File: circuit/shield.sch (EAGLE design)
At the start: 24 parts, among them Q1 BC547, Q2 BC547, Q3 BC547

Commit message: Removed useless pulldown resistors
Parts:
- removed R19: 10k, rcl:R-EU_0204/2V
- removed R20, R21: 10k, rcl:R-EU_0204/7
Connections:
- net GND: no longer R19.2, R20.2, R21.2
- net N$30: no longer R19.1
- net N$31: no longer R20.1
- net N$32: no longer R21.1
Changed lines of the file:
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@@
 <grid distance="0.1" unitdist="inch" unit="inch" style="lines" multiple="1" display="no" altdistance="0.01" altunitdist="inch" altunit="inch"/>
 <layers>
-<layer number="1" name="Top" color="4" fill="1" visible="yes" active="no"/>
-<layer number="16" name="Bottom" color="1" fill="1" visible="yes" active="no"/>
-<layer number="17" name="Pads" color="2" fill="1" visible="yes" active="no"/>
-<layer number="18" name="Vias" color="2" fill="1" visible="yes" active="no"/>
-<layer number="19" name="Unrouted" color="6" fill="1" visible="yes" active="no"/>
-<layer number="20" name="Dimension" color="15" fill="1" visible="yes" active="no"/>
-<layer number="21" name="tPlace" color="7" fill="1" visible="yes" active="no"/>
-<layer number="22" name="bPlace" color="7" fill="1" visible="yes" active="no"/>
-<layer number="23" name="tOrigins" color="15" fill="1" visible="yes" active="no"/>
-<layer number="24" name="bOrigins" color="15" fill="1" visible="yes" active="no"/>
-<layer number="25" name="tNames" color="7" fill="1" visible="yes" active="no"/>
-<layer number="26" name="bNames" color="7" fill="1" visible="yes" active="no"/>
-<layer number="27" name="tValues" color="7" fill="1" visible="yes" active="no"/>
-<layer number="28" name="bValues" color="7" fill="1" visible="yes" active="no"/>
+<layer number="1" name="Top" color="4" fill="1" visible="no" active="no"/>
+<layer number="16" name="Bottom" color="1" fill="1" visible="no" active="no"/>
+<layer number="17" name="Pads" color="2" fill="1" visible="no" active="no"/>
+<layer number="18" name="Vias" color="2" fill="1" visible="no" active="no"/>
+<layer number="19" name="Unrouted" color="6" fill="1" visible="no" active="no"/>
+<layer number="20" name="Dimension" color="15" fill="1" visible="no" active="no"/>
+<layer number="21" name="tPlace" color="7" fill="1" visible="no" active="no"/>
+<layer number="22" name="bPlace" color="7" fill="1" visible="no" active="no"/>
+<layer number="23" name="tOrigins" color="15" fill="1" visible="no" active="no"/>
+<layer number="24" name="bOrigins" color="15" fill="1" visible="no" active="no"/>
+<layer number="25" name="tNames" color="7" fill="1" visible="no" active="no"/>
+<layer number="26" name="bNames" color="7" fill="1" visible="no" active="no"/>
+<layer number="27" name="tValues" color="7" fill="1" visible="no" active="no"/>
+<layer number="28" name="bValues" color="7" fill="1" visible="no" active="no"/>
 <layer number="29" name="tStop" color="7" fill="3" visible="no" active="no"/>
 <layer number="30" name="bStop" color="7" fill="6" visible="no" active="no"/>
@@
 <layer number="35" name="tGlue" color="7" fill="4" visible="no" active="no"/>
 <layer number="36" name="bGlue" color="7" fill="5" visible="no" active="no"/>
-<layer number="37" name="tTest" color="7" fill="1" visible="yes" active="no"/>
-<layer number="38" name="bTest" color="7" fill="1" visible="yes" active="no"/>
+<layer number="37" name="tTest" color="7" fill="1" visible="no" active="no"/>
+<layer number="38" name="bTest" color="7" fill="1" visible="no" active="no"/>
 <layer number="39" name="tKeepout" color="4" fill="11" visible="no" active="no"/>
 <layer number="40" name="bKeepout" color="1" fill="11" visible="no" active="no"/>
@@
 <layer number="44" name="Drills" color="7" fill="1" visible="no" active="no"/>
 <layer number="45" name="Holes" color="7" fill="1" visible="no" active="no"/>
-<layer number="46" name="Milling" color="3" fill="1" visible="yes" active="no"/>
-<layer number="47" name="Measures" color="7" fill="1" visible="yes" active="no"/>
-<layer number="48" name="Document" color="7" fill="1" visible="yes" active="no"/>
-<layer number="49" name="Reference" color="7" fill="1" visible="yes" active="no"/>
-<layer number="51" name="tDocu" color="7" fill="1" visible="yes" active="no"/>
-<layer number="52" name="bDocu" color="7" fill="1" visible="yes" active="no"/>
+<layer number="46" name="Milling" color="3" fill="1" visible="no" active="no"/>
+<layer number="47" name="Measures" color="7" fill="1" visible="no" active="no"/>
+<layer number="48" name="Document" color="7" fill="1" visible="no" active="no"/>
+<layer number="49" name="Reference" color="7" fill="1" visible="no" active="no"/>
+<layer number="51" name="tDocu" color="7" fill="1" visible="no" active="no"/>
+<layer number="52" name="bDocu" color="7" fill="1" visible="no" active="no"/>
 <layer number="91" name="Nets" color="2" fill="1" visible="yes" active="yes"/>
 <layer number="92" name="Busses" color="1" fill="1" visible="yes" active="yes"/>
@@
 <part name="R16" library="rcl" deviceset="R-EU_" device="0204/7" value="1k"/>
 <part name="JP1" library="pinhead" deviceset="PINHD-2X20" device=""/>
-<part name="R19" library="rcl" deviceset="R-EU_" device="0204/2V" value="10k"/>
-<part name="R20" library="rcl" deviceset="R-EU_" device="0204/7" value="10k"/>
-<part name="R21" library="rcl" deviceset="R-EU_" device="0204/7" value="10k"/>
 <part name="D1" library="diode" deviceset="1N4148" device="DO35-7"/>
 <part name="R17" library="rcl" deviceset="R-EU_" device="0204/7" value="470"/>
@@
 <instance part="R16" gate="G$1" x="55.88" y="27.94" rot="R90"/>
 <instance part="JP1" gate="A" x="127" y="25.4"/>
-<instance part="R19" gate="G$1" x="30.48" y="35.56"/>
-<instance part="R20" gate="G$1" x="45.72" y="35.56"/>
-<instance part="R21" gate="G$1" x="60.96" y="35.56"/>
 <instance part="D1" gate="G$1" x="33.02" y="-12.7"/>
 <instance part="R17" gate="G$1" x="33.02" y="-5.08"/>
@@
 <pinref part="GND1" gate="1" pin="GND"/>
 <wire x1="35.56" y1="22.86" x2="35.56" y2="35.56" width="0.1524" layer="91"/>
-<pinref part="R19" gate="G$1" pin="2"/>
-<junction x="35.56" y="35.56"/>
 </segment>
 <segment>
@@
 <pinref part="GND2" gate="1" pin="GND"/>
 <wire x1="50.8" y1="22.86" x2="50.8" y2="35.56" width="0.1524" layer="91"/>
-<pinref part="R20" gate="G$1" pin="2"/>
-<junction x="50.8" y="35.56"/>
 </segment>
 <segment>
@@
 <pinref part="GND3" gate="1" pin="GND"/>
 <wire x1="66.04" y1="22.86" x2="66.04" y2="35.56" width="0.1524" layer="91"/>
-<pinref part="R21" gate="G$1" pin="2"/>
-<junction x="66.04" y="35.56"/>
 </segment>
 <segment>
@@
 <pinref part="Q1" gate="G$1" pin="B"/>
 <pinref part="R14" gate="G$1" pin="2"/>
-<wire x1="25.4" y1="33.02" x2="25.4" y2="35.56" width="0.1524" layer="91"/>
-<wire x1="25.4" y1="35.56" x2="25.4" y2="38.1" width="0.1524" layer="91"/>
-<wire x1="25.4" y1="38.1" x2="25.4" y2="40.64" width="0.1524" layer="91"/>
+<wire x1="25.4" y1="33.02" x2="25.4" y2="40.64" width="0.1524" layer="91"/>
 <wire x1="25.4" y1="40.64" x2="30.48" y2="40.64" width="0.1524" layer="91"/>
-<pinref part="R19" gate="G$1" pin="1"/>
-<junction x="25.4" y="35.56"/>
 </segment>
 </net>
@@
 <pinref part="Q2" gate="G$1" pin="B"/>
 <pinref part="R15" gate="G$1" pin="2"/>
-<wire x1="40.64" y1="33.02" x2="40.64" y2="35.56" width="0.1524" layer="91"/>
-<wire x1="40.64" y1="35.56" x2="40.64" y2="40.64" width="0.1524" layer="91"/>
+<wire x1="40.64" y1="33.02" x2="40.64" y2="40.64" width="0.1524" layer="91"/>
 <wire x1="40.64" y1="40.64" x2="45.72" y2="40.64" width="0.1524" layer="91"/>
-<pinref part="R20" gate="G$1" pin="1"/>
-<junction x="40.64" y="35.56"/>
 </segment>
 </net>
@@
 <pinref part="Q3" gate="G$1" pin="B"/>
 <pinref part="R16" gate="G$1" pin="2"/>
-<wire x1="55.88" y1="33.02" x2="55.88" y2="35.56" width="0.1524" layer="91"/>
-<wire x1="55.88" y1="35.56" x2="55.88" y2="40.64" width="0.1524" layer="91"/>
+<wire x1="55.88" y1="33.02" x2="55.88" y2="40.64" width="0.1524" layer="91"/>
 <wire x1="55.88" y1="40.64" x2="60.96" y2="40.64" width="0.1524" layer="91"/>
-<pinref part="R21" gate="G$1" pin="1"/>
-<junction x="55.88" y="35.56"/>
-</segment>
-</net>
+</segment>
+</net>

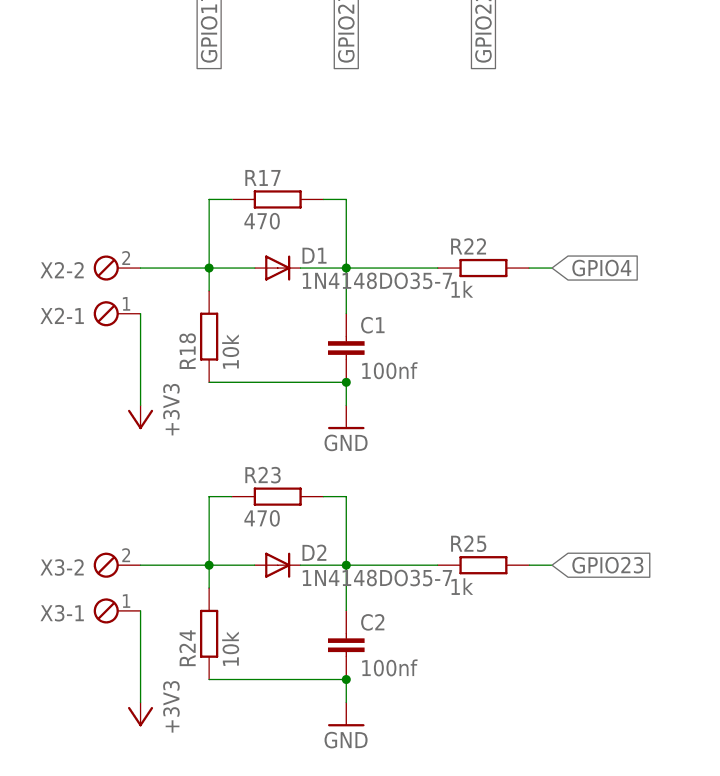
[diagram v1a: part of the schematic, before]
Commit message: moved hardware debounce to software
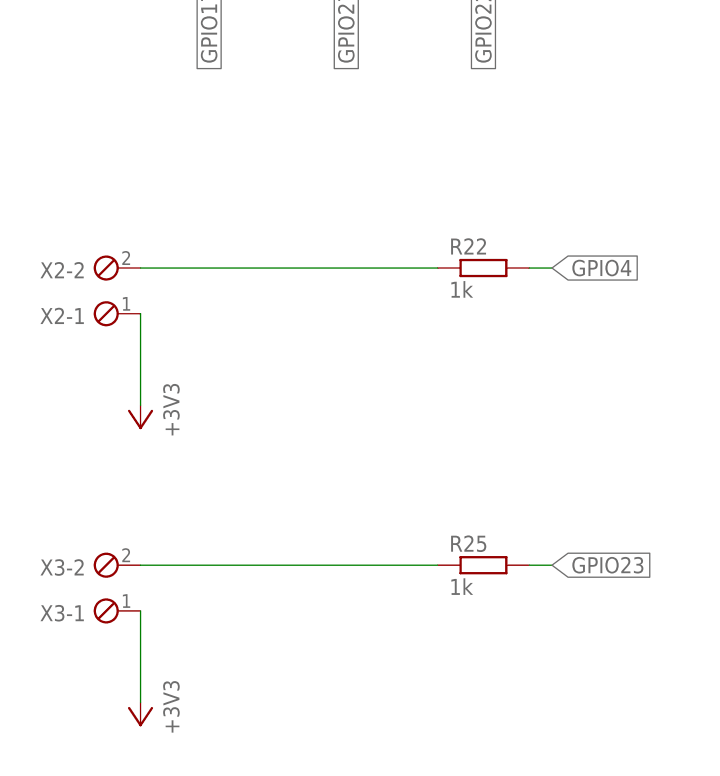
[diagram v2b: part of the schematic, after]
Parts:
- removed C1, C2: 100nf, rcl:C-EU025-025X050
- removed D1, D2: 1N4148DO35-7, diode:1N4148DO35-7
- removed R17, R23: 470, rcl:R-EU_0204/7
- removed R18, R24: 10k, rcl:R-EU_0204/7
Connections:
- removed net N$33: C1.1, D1.C, R17.2, R22.1
- removed net N$35: D2.A, R23.1, R24.2, X3-2.1
- removed net N$36: C2.1, D2.C, R23.2, R25.1
- new net N$1: R25.1, X3-2.1
- net GND: no longer C1.2, C2.2, R18.1, R24.1
- net N$34: now also R22.1; no longer D1.A, R17.1, R18.2
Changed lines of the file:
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@@
 <part name="R16" library="rcl" deviceset="R-EU_" device="0204/7" value="1k"/>
 <part name="JP1" library="pinhead" deviceset="PINHD-2X20" device=""/>
-<part name="D1" library="diode" deviceset="1N4148" device="DO35-7"/>
-<part name="R17" library="rcl" deviceset="R-EU_" device="0204/7" value="470"/>
-<part name="C1" library="rcl" deviceset="C-EU" device="025-025X050" value="100nf"/>
-<part name="R18" library="rcl" deviceset="R-EU_" device="0204/7" value="10k"/>
-<part name="GND5" library="supply1" deviceset="GND" device=""/>
 <part name="R22" library="rcl" deviceset="R-EU_" device="0204/7" value="1k"/>
 <part name="P+4" library="supply1" deviceset="+5V" device=""/>
@@
 <part name="+3V2" library="supply1" deviceset="+3V3" device=""/>
 <part name="+3V3" library="supply1" deviceset="+3V3" device=""/>
-<part name="D2" library="diode" deviceset="1N4148" device="DO35-7"/>
-<part name="R23" library="rcl" deviceset="R-EU_" device="0204/7" value="470"/>
-<part name="C2" library="rcl" deviceset="C-EU" device="025-025X050" value="100nf"/>
-<part name="R24" library="rcl" deviceset="R-EU_" device="0204/7" value="10k"/>
-<part name="GND6" library="supply1" deviceset="GND" device=""/>
 <part name="R25" library="rcl" deviceset="R-EU_" device="0204/7" value="1k"/>
 <part name="GND7" library="supply1" deviceset="GND" device=""/>
@@
 <instance part="R16" gate="G$1" x="55.88" y="27.94" rot="R90"/>
 <instance part="JP1" gate="A" x="127" y="25.4"/>
-<instance part="D1" gate="G$1" x="33.02" y="-12.7"/>
-<instance part="R17" gate="G$1" x="33.02" y="-5.08"/>
-<instance part="C1" gate="G$1" x="40.64" y="-20.32"/>
-<instance part="R18" gate="G$1" x="25.4" y="-20.32" rot="R90"/>
-<instance part="GND5" gate="1" x="40.64" y="-30.48"/>
 <instance part="R22" gate="G$1" x="55.88" y="-12.7"/>
 <instance part="P+4" gate="1" x="144.78" y="48.26" rot="R270"/>
@@
 <instance part="+3V2" gate="G$1" x="17.78" y="-30.48" rot="R180"/>
 <instance part="+3V3" gate="G$1" x="17.78" y="-63.5" rot="R180"/>
-<instance part="D2" gate="G$1" x="33.02" y="-45.72"/>
-<instance part="R23" gate="G$1" x="33.02" y="-38.1"/>
-<instance part="C2" gate="G$1" x="40.64" y="-53.34"/>
-<instance part="R24" gate="G$1" x="25.4" y="-53.34" rot="R90"/>
-<instance part="GND6" gate="1" x="40.64" y="-63.5"/>
 <instance part="R25" gate="G$1" x="55.88" y="-45.72"/>
 <instance part="GND7" gate="1" x="142.24" y="43.18" rot="R90"/>
@@
 </segment>
 <segment>
-<pinref part="C1" gate="G$1" pin="2"/>
-<pinref part="R18" gate="G$1" pin="1"/>
-<wire x1="40.64" y1="-25.4" x2="25.4" y2="-25.4" width="0.1524" layer="91"/>
-<pinref part="GND5" gate="1" pin="GND"/>
-<wire x1="40.64" y1="-27.94" x2="40.64" y2="-25.4" width="0.1524" layer="91"/>
-<junction x="40.64" y="-25.4"/>
-</segment>
-<segment>
-<pinref part="C2" gate="G$1" pin="2"/>
-<pinref part="R24" gate="G$1" pin="1"/>
-<wire x1="40.64" y1="-58.42" x2="25.4" y2="-58.42" width="0.1524" layer="91"/>
-<pinref part="GND6" gate="1" pin="GND"/>
-<wire x1="40.64" y1="-60.96" x2="40.64" y2="-58.42" width="0.1524" layer="91"/>
-<junction x="40.64" y="-58.42"/>
-</segment>
-<segment>
 <pinref part="JP1" gate="A" pin="6"/>
 <pinref part="GND7" gate="1" pin="GND"/>
@@
 <net name="N$34" class="0">
 <segment>
-<pinref part="R18" gate="G$1" pin="2"/>
-<pinref part="D1" gate="G$1" pin="A"/>
-<wire x1="25.4" y1="-15.24" x2="25.4" y2="-12.7" width="0.1524" layer="91"/>
-<wire x1="25.4" y1="-12.7" x2="30.48" y2="-12.7" width="0.1524" layer="91"/>
-<pinref part="R17" gate="G$1" pin="1"/>
-<wire x1="27.94" y1="-5.08" x2="25.4" y2="-5.08" width="0.1524" layer="91"/>
-<wire x1="25.4" y1="-5.08" x2="25.4" y2="-12.7" width="0.1524" layer="91"/>
-<junction x="25.4" y="-12.7"/>
-<wire x1="17.78" y1="-12.7" x2="25.4" y2="-12.7" width="0.1524" layer="91"/>
+<wire x1="17.78" y1="-12.7" x2="50.8" y2="-12.7" width="0.1524" layer="91"/>
 <pinref part="X2" gate="-2" pin="1"/>
-</segment>
-</net>
-<net name="N$33" class="0">
-<segment>
-<pinref part="R17" gate="G$1" pin="2"/>
-<pinref part="C1" gate="G$1" pin="1"/>
-<wire x1="38.1" y1="-5.08" x2="40.64" y2="-5.08" width="0.1524" layer="91"/>
-<wire x1="40.64" y1="-5.08" x2="40.64" y2="-12.7" width="0.1524" layer="91"/>
-<pinref part="D1" gate="G$1" pin="C"/>
-<wire x1="40.64" y1="-12.7" x2="40.64" y2="-17.78" width="0.1524" layer="91"/>
-<wire x1="35.56" y1="-12.7" x2="40.64" y2="-12.7" width="0.1524" layer="91"/>
-<junction x="40.64" y="-12.7"/>
 <pinref part="R22" gate="G$1" pin="1"/>
-<wire x1="40.64" y1="-12.7" x2="50.8" y2="-12.7" width="0.1524" layer="91"/>
 </segment>
 </net>
@@
 </segment>
 </net>
-<net name="N$35" class="0">
-<segment>
-<pinref part="R24" gate="G$1" pin="2"/>
-<pinref part="D2" gate="G$1" pin="A"/>
-<wire x1="25.4" y1="-48.26" x2="25.4" y2="-45.72" width="0.1524" layer="91"/>
-<wire x1="25.4" y1="-45.72" x2="30.48" y2="-45.72" width="0.1524" layer="91"/>
-<pinref part="R23" gate="G$1" pin="1"/>
-<wire x1="27.94" y1="-38.1" x2="25.4" y2="-38.1" width="0.1524" layer="91"/>
-<wire x1="25.4" y1="-38.1" x2="25.4" y2="-45.72" width="0.1524" layer="91"/>
-<junction x="25.4" y="-45.72"/>
-<wire x1="17.78" y1="-45.72" x2="25.4" y2="-45.72" width="0.1524" layer="91"/>
+<net name="N$1" class="0">
+<segment>
 <pinref part="X3" gate="-2" pin="1"/>
-</segment>
-</net>
-<net name="N$36" class="0">
-<segment>
-<pinref part="R23" gate="G$1" pin="2"/>
-<pinref part="C2" gate="G$1" pin="1"/>
-<wire x1="38.1" y1="-38.1" x2="40.64" y2="-38.1" width="0.1524" layer="91"/>
-<wire x1="40.64" y1="-38.1" x2="40.64" y2="-45.72" width="0.1524" layer="91"/>
-<pinref part="D2" gate="G$1" pin="C"/>
-<wire x1="40.64" y1="-45.72" x2="40.64" y2="-50.8" width="0.1524" layer="91"/>
-<wire x1="35.56" y1="-45.72" x2="40.64" y2="-45.72" width="0.1524" layer="91"/>
-<junction x="40.64" y="-45.72"/>
 <pinref part="R25" gate="G$1" pin="1"/>
-<wire x1="40.64" y1="-45.72" x2="50.8" y2="-45.72" width="0.1524" layer="91"/>
-</segment>
-</net>
+<wire x1="17.78" y1="-45.72" x2="50.8" y2="-45.72" width="0.1524" layer="91"/>
+</segment>
+</net>
